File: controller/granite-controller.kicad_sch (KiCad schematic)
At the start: 0 parts

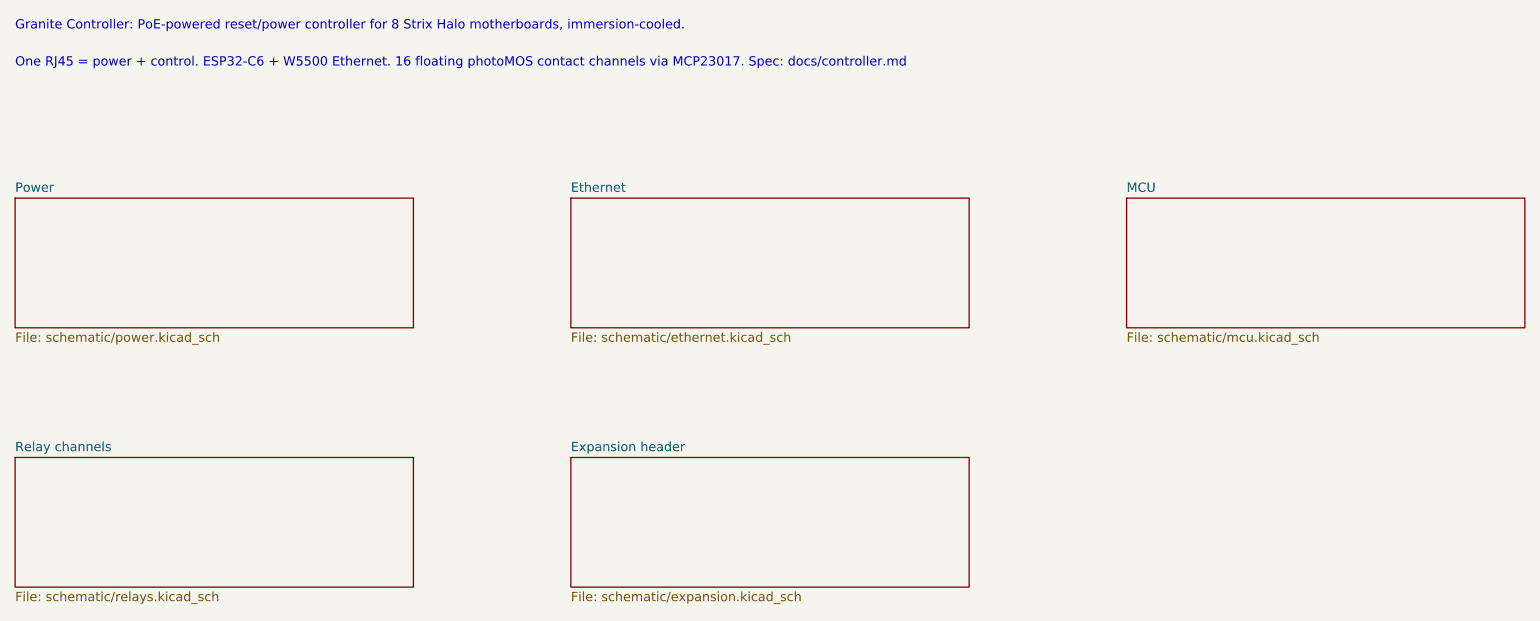
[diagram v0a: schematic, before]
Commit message: controller: rev D schematic - node section (relays sheet: J11-J18, K1-K16, U14-U17 and passives), J8 expansion header network (RN2, U7, F2, D7, R19, EXP_nRESET) and the 19 V input (J3, F3, D1, D8) removed; two 12 V PH 2p inputs J11 / J12 OR-ed by SS34 D10 / D11 with SMAJ15A D12 (C148216), VIN_SENSE divider 68k / 10k; new Plane link sheet: J13 / J14 PH 5p, 2.2k SDA / SCL and 10k EXP_INT pull-ups, 33R series, TPD4E05U06 U19 / U20, TPS2553DBVR load switches U21 / U22 (C55266, R_ILIM 180k, 129-174 mA) with a granite:TPS2553DBV symbol; MCU: plane link on GPIO2/3, TMP1075 and J9 on the local bus GPIO6/7, dry inputs on GPIO10/11/4/15, rev C GPIO4 pull-down gone; title blocks rev D; ERC 0, netlist pin map checked
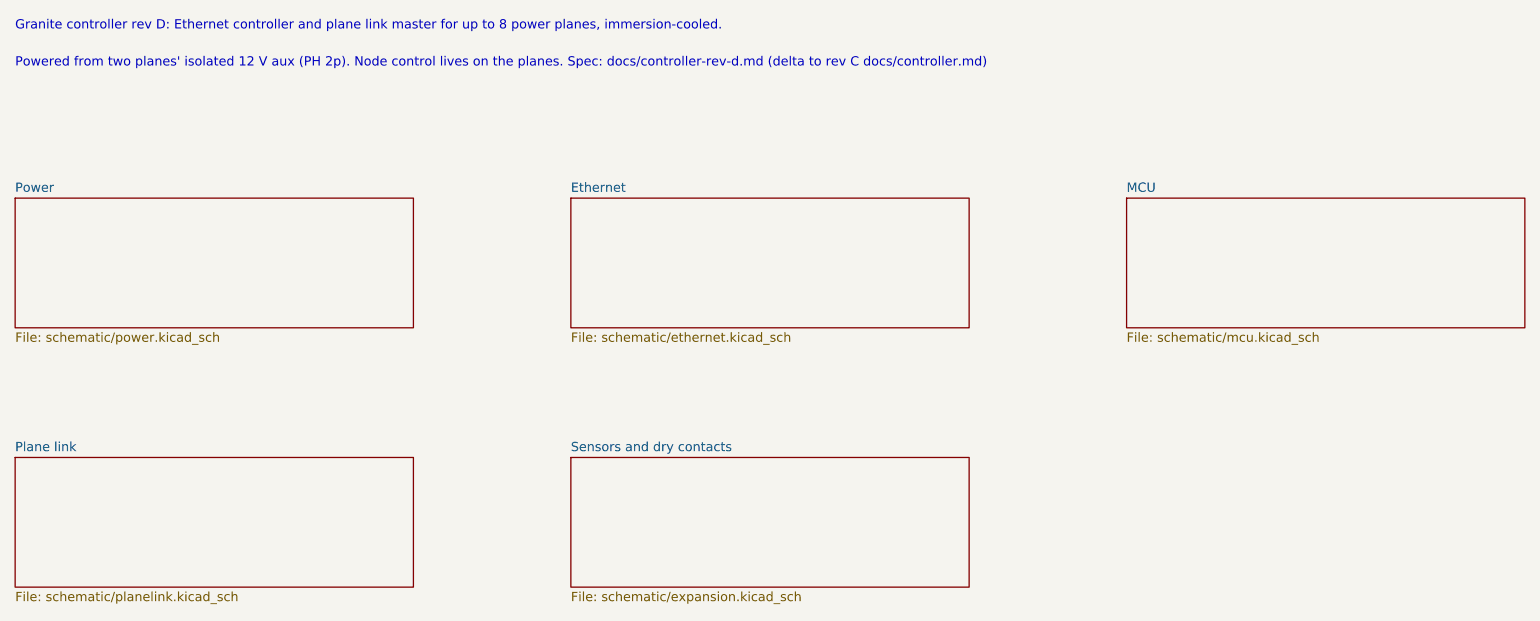
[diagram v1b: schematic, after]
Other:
- sheet Expansion header renamed Sensors and dry contacts
- removed sheet Relay channels
- added sheet Plane link (schematic/planelink.kicad_sch)
- note added: "Granite controller rev D: Ethernet controller and plane link master for up to 8 power planes, immersion-cooled."
- note added: "Powered from two planes' isolated 12 V aux (PH 2p). Node control lives on the planes. Spec: docs/controller-rev-d.md (delta to rev C docs/controller.md)"
- note removed: "Granite Controller: PoE-powered reset/power controller for 8 Strix Halo motherboards, immersion-cooled."
- note removed: "One RJ45 = power + control. ESP32-C6 + W5500 Ethernet. 16 floating photoMOS contact channels via MCP23017. Spec: docs/controller.md"
- title: Granite Controller - MCU and USB -> Granite controller rev D
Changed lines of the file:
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@@
 	(paper "A4")
 	(title_block
-		(title "Granite Controller - MCU and USB")
-		(date "2026-07-09")
-		(rev "C")
-		(comment 1 "PoE-powered reset/power controller for 2x7 Strix Halo motherboards")
-		(comment 2 "STM32H563 + LAN8742A + 802.3af PD, 28x photoMOS channels")
-	)
-	(text "Granite Controller: PoE-powered reset/power controller for 8 Strix Halo motherboards, immersion-cooled."
+		(title "Granite controller rev D")
+		(date "2026-10-30")
+		(rev "D")
+		(comment 1 "Ethernet controller and plane link master for frames with 48 V power planes")
+		(comment 2 "ESP32-C6 + W5500, 2x 12 V in from the planes, 2x plane link (I2C + EXP_INT), probes, dry contacts, Qwiic")
+	)
+	(text "Granite controller rev D: Ethernet controller and plane link master for up to 8 power planes, immersion-cooled."
 		(exclude_from_sim no)
 		(at 31.75 22.86 0)
@@
 		)
 	)
-	(text "One RJ45 = power + control. ESP32-C6 + W5500 Ethernet. 16 floating photoMOS contact channels via MCP23017. Spec: docs/controller.md"
+	(text "Powered from two planes' isolated 12 V aux (PH 2p). Node control lives on the planes. Spec: docs/controller-rev-d.md (delta to rev C docs/controller.md)"
 		(exclude_from_sim no)
 		(at 31.75 27.94 0)
@@
 	)
 	(sheet
-		(at 31.75 81.28)
-		(size 54.61 17.78)
-		(exclude_from_sim no)
-		(in_bom yes)
-		(on_board yes)
-		(dnp no)
-		(fields_autoplaced yes)
-		(stroke
-			(width 0.1524)
-			(type solid)
-		)
-		(fill
-			(color 0 0 0 0)
-		)
-		(property "Sheetname" "Relay channels"
-			(at 31.75 80.5684 0)
-			(show_name no)
-			(do_not_autoplace no)
-			(effects
-				(font
-					(size 1.27 1.27)
-				)
-				(justify left bottom)
-			)
-		)
-		(property "Sheetfile" "schematic/relays.kicad_sch"
-			(at 31.75 99.6484 0)
-			(show_name no)
-			(do_not_autoplace no)
-			(effects
-				(font
-					(size 1.27 1.27)
-				)
-				(justify left top)
-			)
-		)
-		(instances
-			(project "granite-controller"
-				(path "/bd3d1081-8fd5-561e-93ea-9d28b3145149"
-					(page "5")
-				)
-			)
-		)
-	)
-	(sheet
 		(at 107.95 81.28)
 		(size 54.61 17.78)
@@
 			(color 0 0 0 0)
 		)
-		(property "Sheetname" "Expansion header"
+		(property "Sheetname" "Sensors and dry contacts"
 			(at 107.95 80.5684 0)
 			(show_name no)
@@
 			(show_name no)
 			(do_not_autoplace no)
+			(effects
+				(font
+					(size 1.27 1.27)
+				)
+				(justify left top)
+			)
+		)
+		(instances
+			(project "granite-controller"
+				(path "/bd3d1081-8fd5-561e-93ea-9d28b3145149"
+					(page "5")
+				)
+			)
+		)
+	)
+	(sheet
+		(at 31.75 81.28)
+		(size 54.61 17.78)
+		(exclude_from_sim no)
+		(in_bom yes)
+		(on_board yes)
+		(dnp no)
+		(fields_autoplaced yes)
+		(stroke
+			(width 0.1524)
+			(type solid)
+		)
+		(fill
+			(color 0 0 0 0)
+		)
+		(property "Sheetname" "Plane link"
+			(at 31.75 80.5684 0)
+			(show_name no)
+			(do_not_autoplace no)
+			(effects
+				(font
+					(size 1.27 1.27)
+				)
+				(justify left bottom)
+			)
+		)
+		(property "Sheetfile" "schematic/planelink.kicad_sch"
+			(at 31.75 99.6484 0)
+			(show_name no)
+			(do_not_autoplace no)
